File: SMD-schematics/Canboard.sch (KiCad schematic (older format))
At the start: 12 parts, among them J1 Barrel_Jack, J2 Screw_Terminal_01x02, J3 USB_OTG, J4 Conn_Debug, U1 L7805

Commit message: "placing the footprints in PCB design no trakes yet"
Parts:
- J1: footprint Connectors2:JACK_ALIM -> Connectors:JACK_ALIM
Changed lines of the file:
@@
 $EndComp
 $Comp
-L GND #PWR01
+L GND #PWR8
 U 1 1 59E9809C
 P 6900 5700
-F 0 "#PWR01" H 6900 5450 50  0001 C CNN
+F 0 "#PWR8" H 6900 5450 50  0001 C CNN
 F 1 "GND" H 6900 5550 50  0000 C CNN
 F 2 "" H 6900 5700 50  0001 C CNN
@@
 $EndComp
 $Comp
-L +5V #PWR02
+L +5V #PWR10
 U 1 1 59E980EB
 P 7800 5000
-F 0 "#PWR02" H 7800 4850 50  0001 C CNN
+F 0 "#PWR10" H 7800 4850 50  0001 C CNN
 F 1 "+5V" H 7800 5140 50  0000 C CNN
 F 2 "" H 7800 5000 50  0001 C CNN
@@
 $EndComp
 $Comp
-L +12V #PWR03
+L +12V #PWR7
 U 1 1 59E981FB
 P 6450 4700
-F 0 "#PWR03" H 6450 4550 50  0001 C CNN
+F 0 "#PWR7" H 6450 4550 50  0001 C CNN
 F 1 "+12V" H 6450 4840 50  0000 C CNN
 F 2 "" H 6450 4700 50  0001 C CNN
@@
 $EndComp
 $Comp
-L GND #PWR04
+L GND #PWR9
 U 1 1 59EFD8EA
 P 7500 3900
-F 0 "#PWR04" H 7500 3650 50  0001 C CNN
+F 0 "#PWR9" H 7500 3650 50  0001 C CNN
 F 1 "GND" H 7500 3750 50  0000 C CNN
 F 2 "" H 7500 3900 50  0001 C CNN
@@
 $EndComp
 $Comp
-L +5V #PWR05
+L +5V #PWR11
 U 1 1 59EFDA47
 P 7950 3400
-F 0 "#PWR05" H 7950 3250 50  0001 C CNN
+F 0 "#PWR11" H 7950 3250 50  0001 C CNN
 F 1 "+5V" H 7950 3540 50  0000 C CNN
 F 2 "" H 7950 3400 50  0001 C CNN
@@
 $EndComp
 $Comp
-L GND #PWR06
+L GND #PWR2
 U 1 1 59F00424
 P 1800 3600
-F 0 "#PWR06" H 1800 3350 50  0001 C CNN
+F 0 "#PWR2" H 1800 3350 50  0001 C CNN
 F 1 "GND" H 1800 3450 50  0000 C CNN
 F 2 "" H 1800 3600 50  0001 C CNN
@@
 $EndComp
 $Comp
-L +12V #PWR07
+L +12V #PWR1
 U 1 1 59F004A7
 P 1800 3300
-F 0 "#PWR07" H 1800 3150 50  0001 C CNN
+F 0 "#PWR1" H 1800 3150 50  0001 C CNN
 F 1 "+12V" H 1800 3440 50  0000 C CNN
 F 2 "" H 1800 3300 50  0001 C CNN
@@
 $EndComp
 $Comp
-L +5V #PWR08
+L +5V #PWR6
 U 1 1 59F00FFA
 P 3150 1900
-F 0 "#PWR08" H 3150 1750 50  0001 C CNN
+F 0 "#PWR6" H 3150 1750 50  0001 C CNN
 F 1 "+5V" H 3150 2040 50  0000 C CNN
 F 2 "" H 3150 1900 50  0001 C CNN
@@
 $EndComp
 $Comp
-L GND #PWR09
+L GND #PWR5
 U 1 1 59F0110C
 P 2650 2750
-F 0 "#PWR09" H 2650 2500 50  0001 C CNN
+F 0 "#PWR5" H 2650 2500 50  0001 C CNN
 F 1 "GND" H 2650 2600 50  0000 C CNN
 F 2 "" H 2650 2750 50  0001 C CNN
@@
 F 0 "J1" H 1100 2310 50  0000 C CNN
 F 1 "Barrel_Jack" H 1100 1925 50  0000 C CNN
-F 2 "Connectors2:JACK_ALIM" H 1150 2060 50  0001 C CNN
+F 2 "Connectors:JACK_ALIM" H 1150 2060 50  0001 C CNN
 F 3 "" H 1150 2060 50  0001 C CNN
 	1    1100 2100
@@
 $EndComp
 $Comp
-L GND #PWR010
+L GND #PWR4
 U 1 1 59F017C3
 P 1900 2200
-F 0 "#PWR010" H 1900 1950 50  0001 C CNN
+F 0 "#PWR4" H 1900 1950 50  0001 C CNN
 F 1 "GND" H 1900 2050 50  0000 C CNN
 F 2 "" H 1900 2200 50  0001 C CNN
@@
 $EndComp
 $Comp
-L +12V #PWR011
+L +12V #PWR3
 U 1 1 59F017C9
 P 1900 1750
-F 0 "#PWR011" H 1900 1600 50  0001 C CNN
+F 0 "#PWR3" H 1900 1600 50  0001 C CNN
 F 1 "+12V" H 1900 1890 50  0000 C CNN
 F 2 "" H 1900 1750 50  0001 C CNN
@@
 $EndComp
 $Comp
-L GND #PWR012
+L GND #PWR12
 U 1 1 59F05511
 P 10250 1900
-F 0 "#PWR012" H 10250 1650 50  0001 C CNN
+F 0 "#PWR12" H 10250 1650 50  0001 C CNN
 F 1 "GND" H 10250 1750 50  0000 C CNN
 F 2 "" H 10250 1900 50  0001 C CNN
@@
 $EndComp
 $Comp
-L PWR_FLAG #FLG013
+L PWR_FLAG #FLG1
 U 1 1 59F0AA68
 P 1450 3450
-F 0 "#FLG013" H 1450 3525 50  0001 C CNN
+F 0 "#FLG1" H 1450 3525 50  0001 C CNN
 F 1 "PWR_FLAG" H 1450 3600 50  0000 C CNN
 F 2 "" H 1450 3450 50  0001 C CNN
@@
 $EndComp
 $Comp
-L PWR_FLAG #FLG014
+L PWR_FLAG #FLG2
 U 1 1 59F032C2
 P 2050 3150
-F 0 "#FLG014" H 2050 3225 50  0001 C CNN
+F 0 "#FLG2" H 2050 3225 50  0001 C CNN
 F 1 "PWR_FLAG" H 2050 3300 50  0000 C CNN
 F 2 "" H 2050 3150 50  0001 C CNN
@@
 $EndComp
 $Comp
-L PWR_FLAG #FLG015
+L PWR_FLAG #FLG3
 U 1 1 5A2E2E0E
 P 3000 1650
-F 0 "#FLG015" H 3000 1725 50  0001 C CNN
+F 0 "#FLG3" H 3000 1725 50  0001 C CNN
 F 1 "PWR_FLAG" H 3000 1800 50  0000 C CNN
 F 2 "" H 3000 1650 50  0001 C CNN

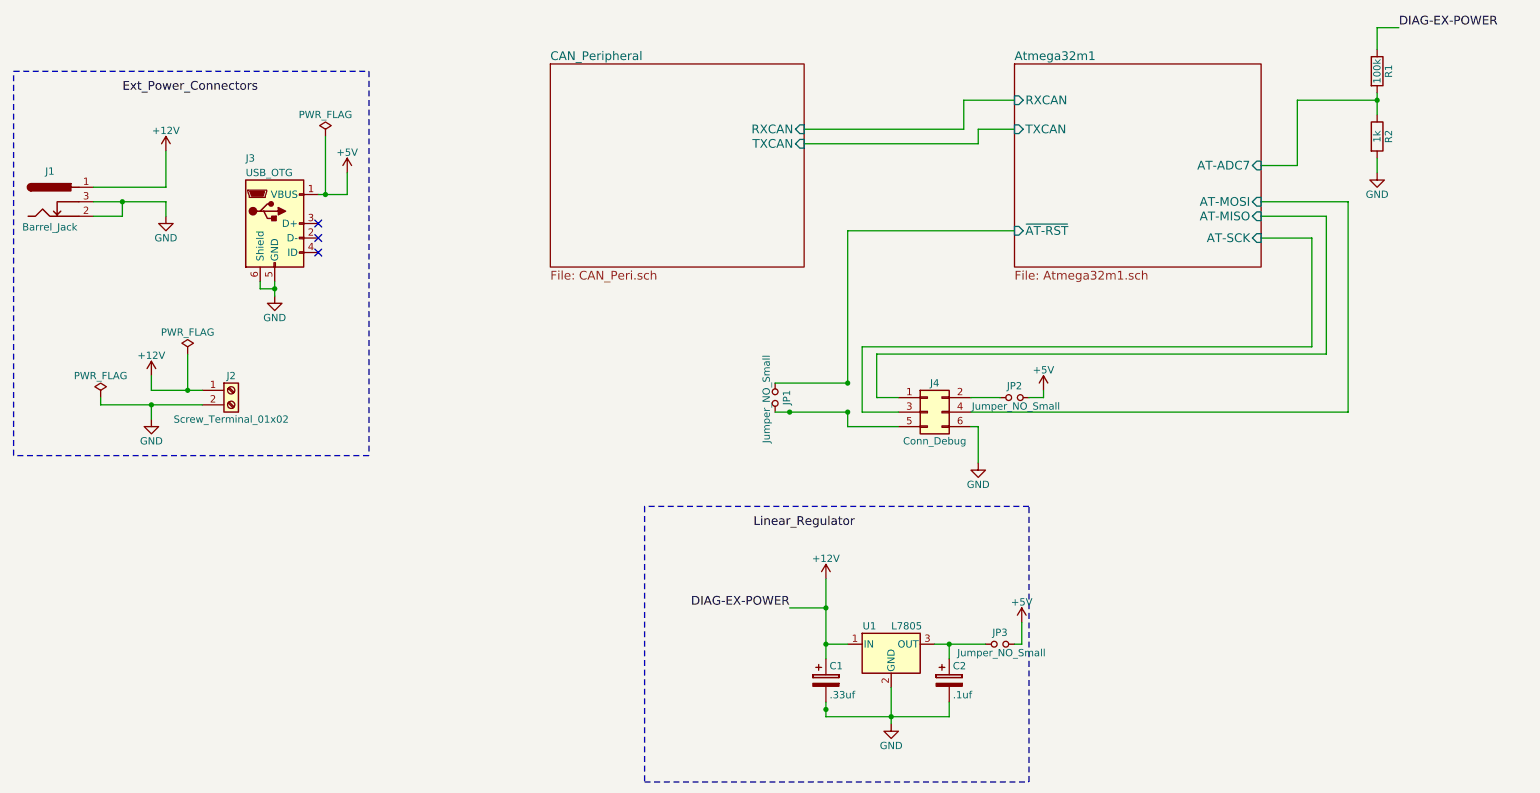
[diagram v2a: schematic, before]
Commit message: Updating Schematics: removing DB9 connectors and usart Transceiver
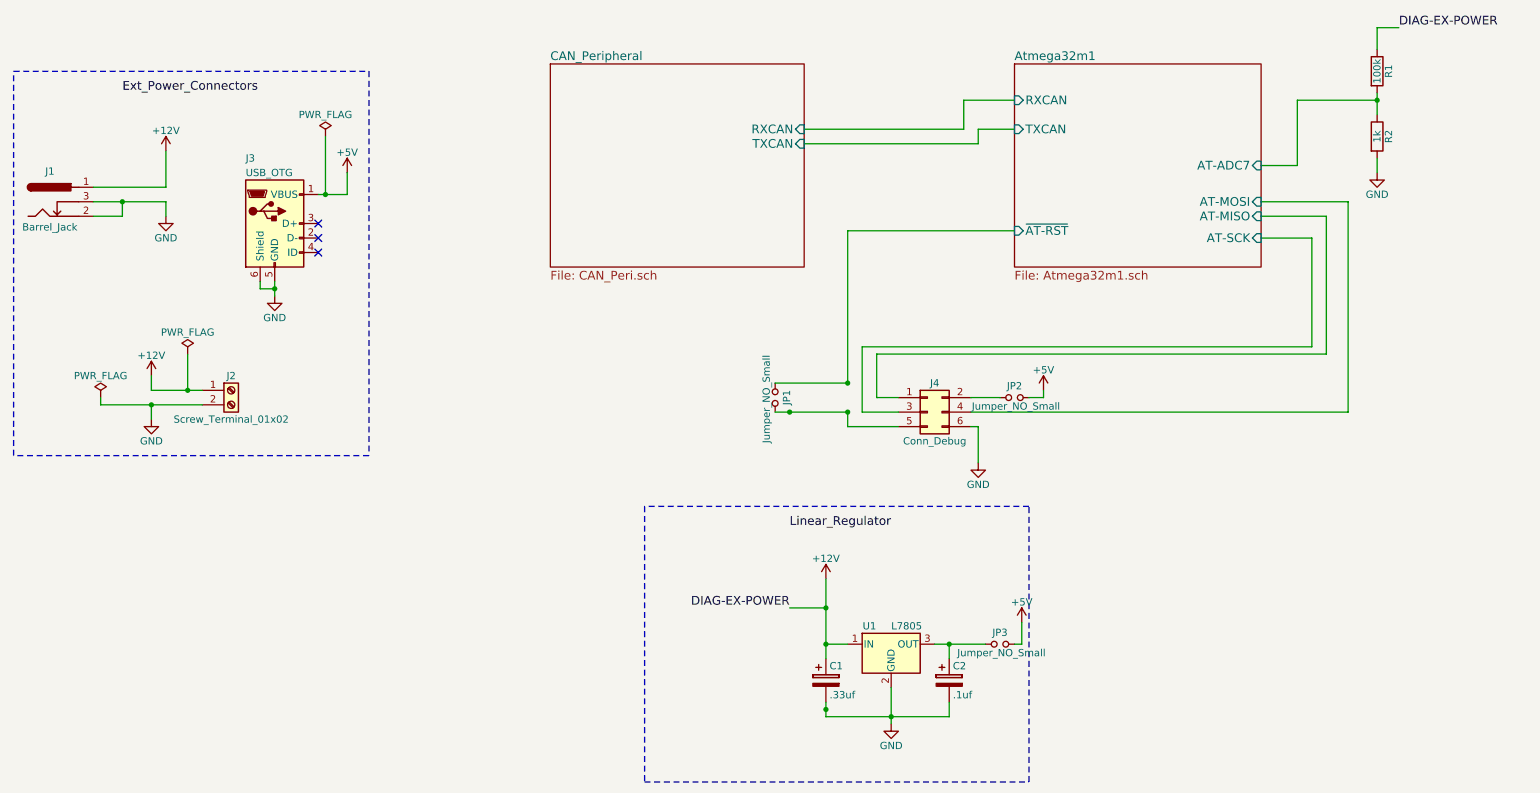
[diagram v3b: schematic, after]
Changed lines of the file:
@@
 Text Label 1600 1350 0    60   ~ 0
 Ext_Power_Connectors
-Text Label 5950 4350 0    60   ~ 0
+Text Label 6200 4350 0    60   ~ 0
 Linear_Regulator
 $Comp
@@
 $EndComp
 Wire Wire Line
-	6900 5450 6900 5700
+	6900 5450 6900 5650
+Wire Wire Line
+	6900 5650 6900 5700
 Connection ~ 7300 5150
 Wire Wire Line
-	6450 5650 7300 5650
+	6450 5650 6900 5650
+Wire Wire Line
+	6900 5650 7300 5650
 Wire Wire Line
 	7300 5650 7300 5550
 Connection ~ 6900 5650
 Wire Wire Line
-	6450 4700 6450 5250
+	6450 4700 6450 4900
 Wire Wire Line
-	6450 5550 6450 5650
+	6450 4900 6450 5150
+Wire Wire Line
+	6450 5150 6450 5250
+Wire Wire Line
+	6450 5550 6450 5600
+Wire Wire Line
+	6450 5600 6450 5650
 Connection ~ 6450 5150
 Connection ~ 6450 4900
@@
 	6100 3350 6600 3350
 Wire Wire Line
-	6100 3550 6600 3550
+	6100 3550 6200 3550
+Wire Wire Line
+	6200 3550 6600 3550
 Connection ~ 6200 3550
 Connection ~ 6600 3350
@@
 	6200 4900 6450 4900
 Wire Wire Line
-	1800 3400 2150 3400
+	1800 3400 2050 3400
 Wire Wire Line
-	1450 3500 2150 3500
+	2050 3400 2150 3400
+Wire Wire Line
+	1450 3500 1800 3500
+Wire Wire Line
+	1800 3500 2150 3500
 Wire Wire Line
 	1800 3400 1800 3300
@@
 	3150 2050 3150 1900
 Wire Wire Line
-	2950 2050 3150 2050
+	2950 2050 3000 2050
 Wire Wire Line
-	2650 2650 2650 2750
+	3000 2050 3150 2050
+Wire Wire Line
+	2650 2650 2650 2700
+Wire Wire Line
+	2650 2700 2650 2750
 Wire Wire Line
 	1400 2000 1900 2000
 Wire Wire Line
-	1400 2100 1900 2100
+	1400 2100 1600 2100
+Wire Wire Line
+	1600 2100 1900 2100
 Wire Wire Line
 	1900 2000 1900 1750
@@
 	10250 1900 10250 1800
 Wire Wire Line
-	10250 1350 10250 1500
+	10250 1350 10250 1400
+Wire Wire Line
+	10250 1400 10250 1500
 Wire Wire Line
 	10250 900  10400 900
@@
 	6450 5150 6600 5150
 Wire Wire Line
-	7200 5150 7550 5150
+	7200 5150 7300 5150
+Wire Wire Line
+	7300 5150 7550 5150
 Connection ~ 6450 5600
 Wire Wire Line

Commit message: adding lin circuit to the schematic
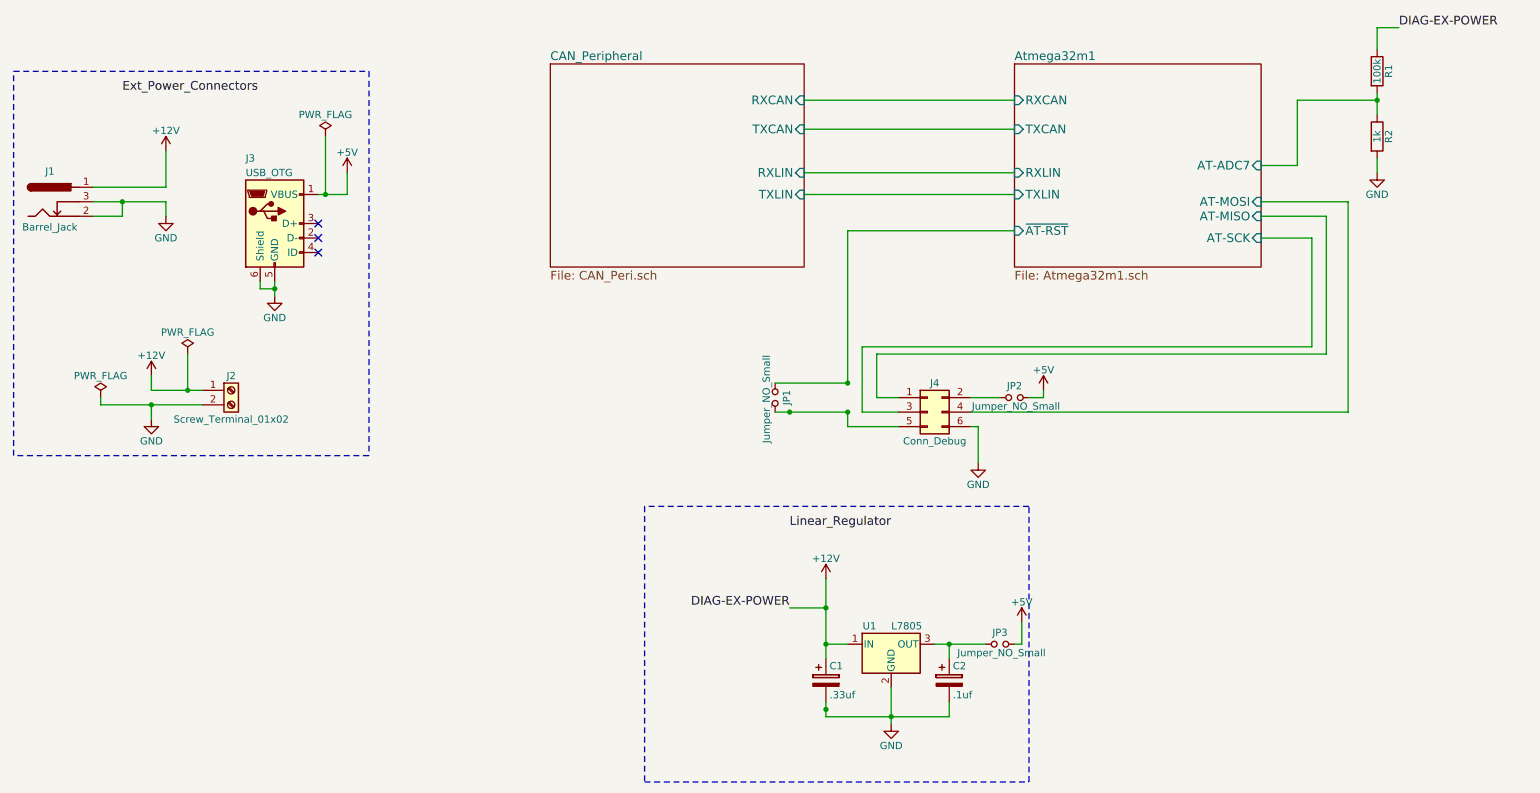
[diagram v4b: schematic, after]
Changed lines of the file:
@@
 LIBS:contrib
 LIBS:valves
+LIBS:mcp2021
+LIBS:diod
+LIBS:diode
+LIBS:Diode1
 LIBS:Canboard-cache
 EELAYER 25 0
@@
 F7 "TXCAN" I L 7750 1600 60
 F8 "RXCAN" I L 7750 1400 60
+F9 "RXLIN" I L 7750 1900 60
+F10 "TXLIN" I L 7750 2050 60
 $EndSheet
 $Comp
@@
 	1    0    0    -1
 $EndComp
-Wire Wire Line
-	6900 5450 6900 5650
-Wire Wire Line
-	6900 5650 6900 5700
-Connection ~ 7300 5150
-Wire Wire Line
-	6450 5650 6900 5650
-Wire Wire Line
-	6900 5650 7300 5650
-Wire Wire Line
-	7300 5650 7300 5550
-Connection ~ 6900 5650
-Wire Wire Line
-	6450 4700 6450 4900
-Wire Wire Line
-	6450 4900 6450 5150
-Wire Wire Line
-	6450 5150 6450 5250
-Wire Wire Line
-	6450 5550 6450 5600
-Wire Wire Line
-	6450 5600 6450 5650
-Connection ~ 6450 5150
-Connection ~ 6450 4900
-Wire Wire Line
-	6300 1600 7400 1600
-Wire Wire Line
-	7400 1600 7400 1400
-Wire Wire Line
-	7400 1400 7750 1400
-Wire Wire Line
-	6300 1700 7500 1700
-Wire Wire Line
-	7500 1700 7500 1600
-Wire Wire Line
-	7500 1600 7750 1600
-Wire Wire Line
-	7450 3650 7500 3650
-Wire Wire Line
-	7500 3650 7500 3900
-Wire Wire Line
-	7450 3450 7650 3450
-Wire Wire Line
-	7450 3550 10050 3550
-Wire Wire Line
-	6800 3450 6950 3450
-Wire Wire Line
-	6700 3550 6950 3550
-Wire Wire Line
-	7750 2300 6600 2300
-Wire Wire Line
-	6600 3650 6950 3650
-Wire Wire Line
-	6100 3350 6600 3350
-Wire Wire Line
-	6100 3550 6200 3550
-Wire Wire Line
-	6200 3550 6600 3550
-Connection ~ 6200 3550
-Connection ~ 6600 3350
-Connection ~ 6600 3550
-Wire Wire Line
-	6600 3350 6600 2300
-Wire Wire Line
-	6600 3550 6600 3650
-Wire Wire Line
-	6200 4900 6450 4900
-Wire Wire Line
-	1800 3400 2050 3400
-Wire Wire Line
-	2050 3400 2150 3400
-Wire Wire Line
-	1450 3500 1800 3500
-Wire Wire Line
-	1800 3500 2150 3500
-Wire Wire Line
-	1800 3400 1800 3300
-Wire Wire Line
-	1800 3500 1800 3600
-Wire Wire Line
-	3150 2050 3150 1900
-Wire Wire Line
-	2950 2050 3000 2050
-Wire Wire Line
-	3000 2050 3150 2050
-Wire Wire Line
-	2650 2650 2650 2700
-Wire Wire Line
-	2650 2700 2650 2750
-Wire Wire Line
-	1400 2000 1900 2000
-Wire Wire Line
-	1400 2100 1600 2100
-Wire Wire Line
-	1600 2100 1900 2100
-Wire Wire Line
-	1900 2000 1900 1750
-Wire Wire Line
-	1900 2100 1900 2200
-Wire Wire Line
-	1400 2200 1600 2200
-Wire Wire Line
-	1600 2200 1600 2100
-Connection ~ 1600 2100
-Wire Wire Line
-	2050 3150 2050 3400
-Connection ~ 2050 3400
-Wire Wire Line
-	10250 900  10250 1050
-Wire Wire Line
-	10250 1900 10250 1800
-Wire Wire Line
-	10250 1350 10250 1400
-Wire Wire Line
-	10250 1400 10250 1500
-Wire Wire Line
-	10250 900  10400 900
-Wire Wire Line
-	9700 1400 10250 1400
-Connection ~ 10250 1400
-Wire Wire Line
-	6450 5150 6600 5150
-Wire Wire Line
-	7200 5150 7300 5150
-Wire Wire Line
-	7300 5150 7550 5150
-Connection ~ 6450 5600
-Wire Wire Line
-	1450 3450 1450 3500
-Connection ~ 1800 3500
-Wire Notes Line
-	850  1200 3300 1200
-Wire Notes Line
-	3300 1200 3300 3850
-Wire Notes Line
-	3300 3850 850  3850
-Wire Notes Line
-	850  3850 850  1200
-Wire Notes Line
-	7850 4200 5200 4200
-Wire Notes Line
-	5200 4200 5200 6100
-Wire Notes Line
-	5200 6100 7850 6100
-Wire Notes Line
-	7850 6100 7850 4200
-Wire Wire Line
-	2550 2650 2550 2700
-Wire Wire Line
-	2550 2700 2650 2700
-Connection ~ 2650 2700
-Wire Wire Line
-	7800 5000 7800 5150
-Wire Wire Line
-	7800 5150 7750 5150
-Wire Wire Line
-	7300 5150 7300 5250
-Wire Wire Line
-	3000 1650 3000 2050
-Connection ~ 3000 2050
-Wire Wire Line
-	9700 1400 9700 1850
-Wire Wire Line
-	9700 1850 9450 1850
-Wire Wire Line
-	9450 2100 10050 2100
-Wire Wire Line
-	10050 2100 10050 3550
-Wire Wire Line
-	7950 3400 7950 3450
-Wire Wire Line
-	7950 3450 7850 3450
-Wire Wire Line
-	9450 2200 9900 2200
-Wire Wire Line
-	9900 2200 9900 3150
-Wire Wire Line
-	9900 3150 6800 3150
-Wire Wire Line
-	6800 3150 6800 3450
-Wire Wire Line
-	6700 3550 6700 3100
-Wire Wire Line
-	6700 3100 9800 3100
-Wire Wire Line
-	9800 3100 9800 2350
-Wire Wire Line
-	9800 2350 9450 2350
 $Sheet
 S 4550 1150 1750 1400
@@
 F0 "CAN_Peripheral" 60
 F1 "CAN_Peri.sch" 60
-F2 "RXCAN" I R 6300 1600 60
-F3 "TXCAN" I R 6300 1700 60
+F2 "RXCAN" I R 6300 1400 60
+F3 "TXCAN" I R 6300 1600 60
+F4 "RXLIN" I R 6300 1900 60
+F5 "TXLIN" I R 6300 2050 60
 $EndSheet
+Wire Wire Line
+	6900 5450 6900 5700
+Connection ~ 7300 5150
+Wire Wire Line
+	6450 5650 7300 5650
+Wire Wire Line
+	7300 5650 7300 5550
+Connection ~ 6900 5650
+Wire Wire Line
+	6450 4700 6450 5250
+Wire Wire Line
+	6450 5550 6450 5650
+Connection ~ 6450 5150
+Connection ~ 6450 4900
+Wire Wire Line
+	6300 1400 7750 1400
+Wire Wire Line
+	6300 1600 7750 1600
+Wire Wire Line
+	7450 3650 7500 3650
+Wire Wire Line
+	7500 3650 7500 3900
+Wire Wire Line
+	7450 3450 7650 3450
+Wire Wire Line
+	7450 3550 10050 3550
+Wire Wire Line
+	6800 3450 6950 3450
+Wire Wire Line
+	6700 3550 6950 3550
+Wire Wire Line
+	7750 2300 6600 2300
+Wire Wire Line
+	6600 3650 6950 3650
+Wire Wire Line
+	6100 3350 6600 3350
+Wire Wire Line
+	6100 3550 6600 3550
+Connection ~ 6200 3550
+Connection ~ 6600 3350
+Connection ~ 6600 3550
+Wire Wire Line
+	6600 3350 6600 2300
+Wire Wire Line
+	6600 3550 6600 3650
+Wire Wire Line
+	6200 4900 6450 4900
+Wire Wire Line
+	1800 3400 2150 3400
+Wire Wire Line
+	1450 3500 2150 3500
+Wire Wire Line
+	1800 3400 1800 3300
+Wire Wire Line
+	1800 3500 1800 3600
+Wire Wire Line
+	3150 2050 3150 1900
+Wire Wire Line
+	2950 2050 3150 2050
+Wire Wire Line
+	2650 2650 2650 2750
+Wire Wire Line
+	1400 2000 1900 2000
+Wire Wire Line
+	1400 2100 1900 2100
+Wire Wire Line
+	1900 2000 1900 1750
+Wire Wire Line
+	1900 2100 1900 2200
+Wire Wire Line
+	1400 2200 1600 2200
+Wire Wire Line
+	1600 2200 1600 2100
+Connection ~ 1600 2100
+Wire Wire Line
+	2050 3150 2050 3400
+Connection ~ 2050 3400
+Wire Wire Line
+	10250 900  10250 1050
+Wire Wire Line
+	10250 1900 10250 1800
+Wire Wire Line
+	10250 1350 10250 1500
+Wire Wire Line
+	10250 900  10400 900
+Wire Wire Line
+	9700 1400 10250 1400
+Connection ~ 10250 1400
+Wire Wire Line
+	6450 5150 6600 5150
+Wire Wire Line
+	7200 5150 7550 5150
+Connection ~ 6450 5600
+Wire Wire Line
+	1450 3450 1450 3500
+Connection ~ 1800 3500
+Wire Notes Line
+	850  1200 3300 1200
+Wire Notes Line
+	3300 1200 3300 3850
+Wire Notes Line
+	3300 3850 850  3850
+Wire Notes Line
+	850  3850 850  1200
+Wire Notes Line
+	7850 4200 5200 4200
+Wire Notes Line
+	5200 4200 5200 6100
+Wire Notes Line
+	5200 6100 7850 6100
+Wire Notes Line
+	7850 6100 7850 4200
+Wire Wire Line
+	2550 2650 2550 2700
+Wire Wire Line
+	2550 2700 2650 2700
+Connection ~ 2650 2700
+Wire Wire Line
+	7800 5000 7800 5150
+Wire Wire Line
+	7800 5150 7750 5150
+Wire Wire Line
+	7300 5150 7300 5250
+Wire Wire Line
+	3000 1650 3000 2050
+Connection ~ 3000 2050
+Wire Wire Line
+	9700 1400 9700 1850
+Wire Wire Line
+	9700 1850 9450 1850
+Wire Wire Line
+	9450 2100 10050 2100
+Wire Wire Line
+	10050 2100 10050 3550
+Wire Wire Line
+	7950 3400 7950 3450
+Wire Wire Line
+	7950 3450 7850 3450
+Wire Wire Line
+	9450 2200 9900 2200
+Wire Wire Line
+	9900 2200 9900 3150
+Wire Wire Line
+	9900 3150 6800 3150
+Wire Wire Line
+	6800 3150 6800 3450
+Wire Wire Line
+	6700 3550 6700 3100
+Wire Wire Line
+	6700 3100 9800 3100
+Wire Wire Line
+	9800 3100 9800 2350
+Wire Wire Line
+	9800 2350 9450 2350
+Wire Wire Line
+	7750 1900 6300 1900
+Wire Wire Line
+	6300 2050 7750 2050
 $EndSCHEMATC
